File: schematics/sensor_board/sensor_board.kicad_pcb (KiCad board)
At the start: 2 copper layers, 17.5 x 18 mm, 19 parts, among them J1 Conn_01x06_Pin, J2 Conn_01x05_Pin, Y1 Crystal

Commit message: Added resistor to the interrupt signal.
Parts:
- added R10: 10k, Resistor_SMD:R_0603_1608Metric_Pad0.98x0.95mm_HandSolder, F.Cu at (111.5, 72.9)
- moved R8 3.51 mm to (114.5, 73.2), turned to 90 degrees
- moved R9 2.24 mm to (116.0, 70.9), turned to -90 degrees
- moved R7 2.19 mm to (114.2, 73.2)
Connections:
- U1 pad 14: /intn -> Net-(U1-H_INTN)
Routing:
- net GND: track 100.2 -> 82.5 mm, vias 4 -> 3
- net Net-(U1-H_INTN): track 0.00 -> 15.4 mm
- net /intn: track 11.5 -> 3.12 mm, vias 2 -> 0
- net /sda: track 22.5 -> 27.5 mm
- net VDD: track 60.3 -> 63.3 mm, vias 6 -> 5
- net /scl: track 23.4 -> 25.2 mm
- net unconnected-(U1-NC-Pad7): track 2.34 -> 1.42 mm
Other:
- board size 17.5 x 18 mm -> 17.5 x 21 mm

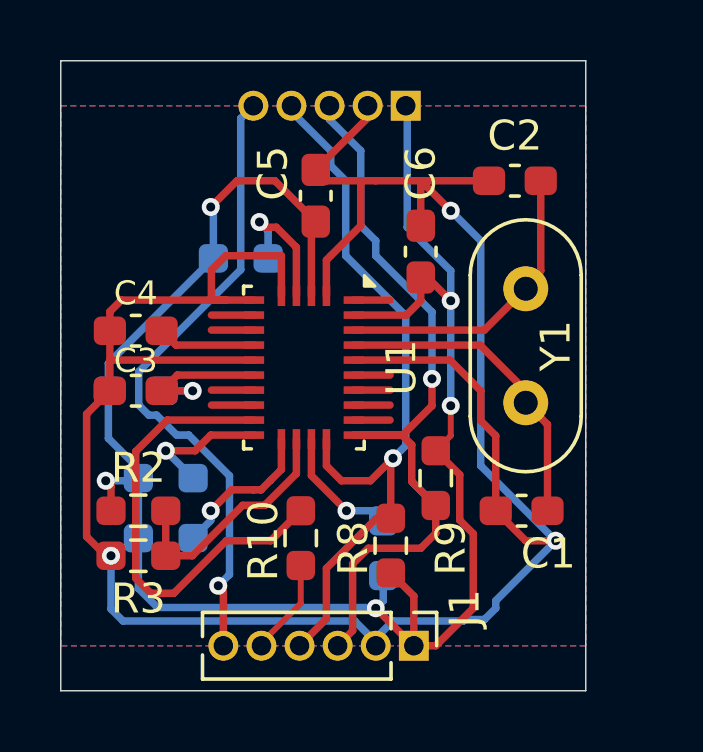
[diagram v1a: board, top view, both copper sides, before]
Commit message: Selarated INT, SCL and SDA lines with GND and VDD so that crosstalk is reduced
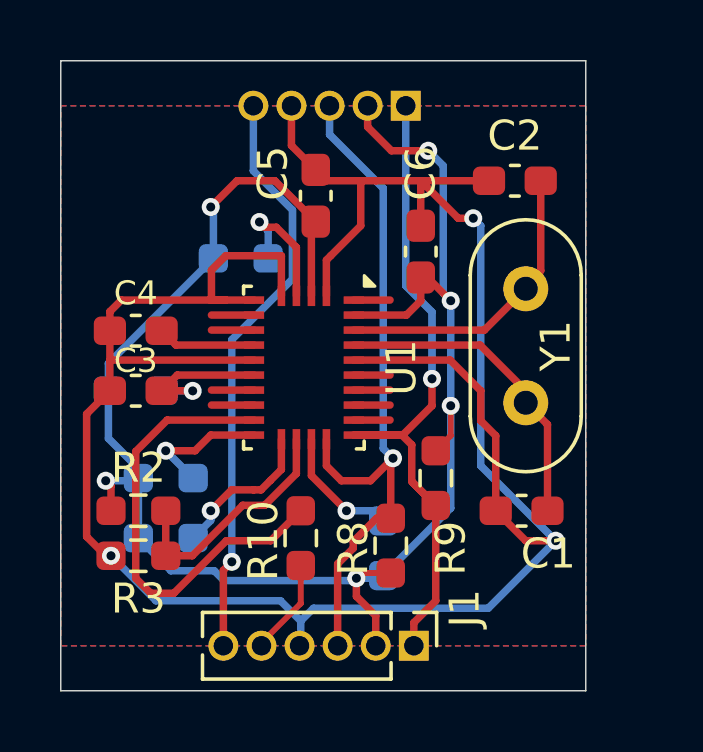
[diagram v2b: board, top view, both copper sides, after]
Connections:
- J1 pad 1: VDD -> /sda
- J1 pad 2: GND -> VDD
- J1 pad 3: /sda -> /scl
- J1 pad 4: /scl -> GND
- J2 pad 1: VDD -> /sda
- J2 pad 2: GND -> VDD
- J2 pad 3: /sda -> /scl
- J2 pad 4: /scl -> GND
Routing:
- net VDD: track 63.3 -> 59.9 mm, vias 5 -> 6
- net /sda: track 27.5 -> 24.5 mm
- net /intn_next: track 21.8 -> 19.8 mm
- net /scl: track 25.2 -> 23.7 mm
- net GND: track 82.5 -> 81.7 mm
